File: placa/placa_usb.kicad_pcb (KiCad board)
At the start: 2 copper layers, 52.5 x 17 mm, 22 parts, among them IC1 ATMEGA16U2, P1 USB_A, P2 CONN_02X05, P3 CONN_01X06, U1 LD1117S33TR, U2 TXB0106, X1 8MHz

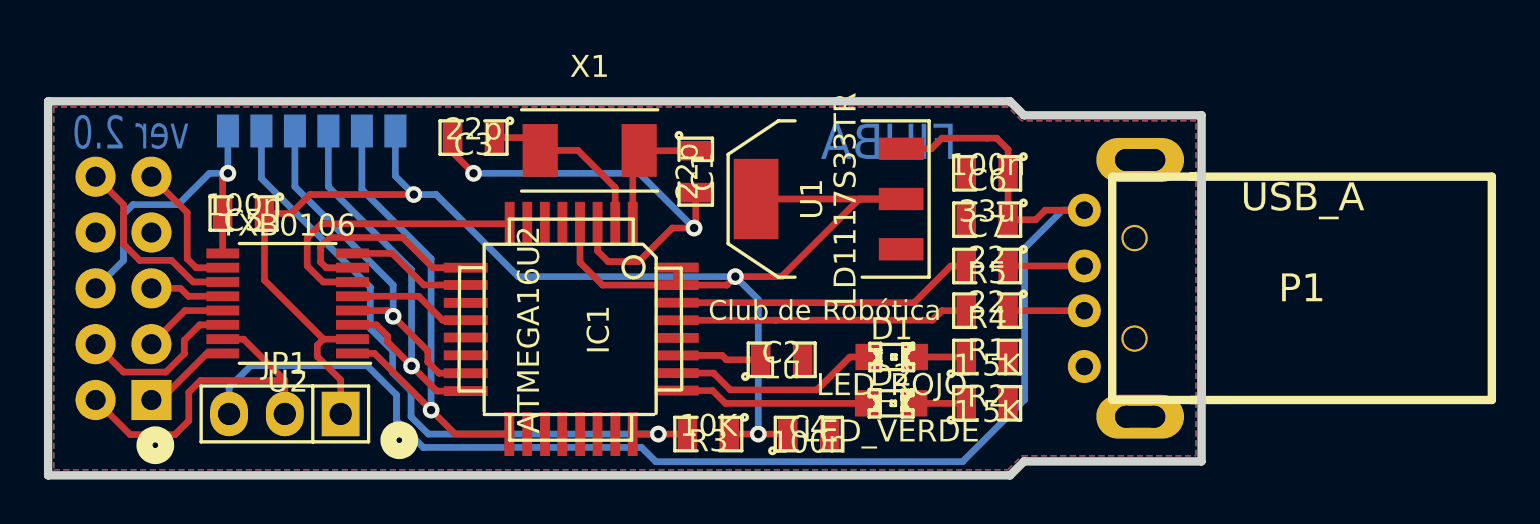
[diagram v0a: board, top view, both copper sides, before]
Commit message: primera version de la placa en componentes smd, queda verificar los tamaños de los footprint
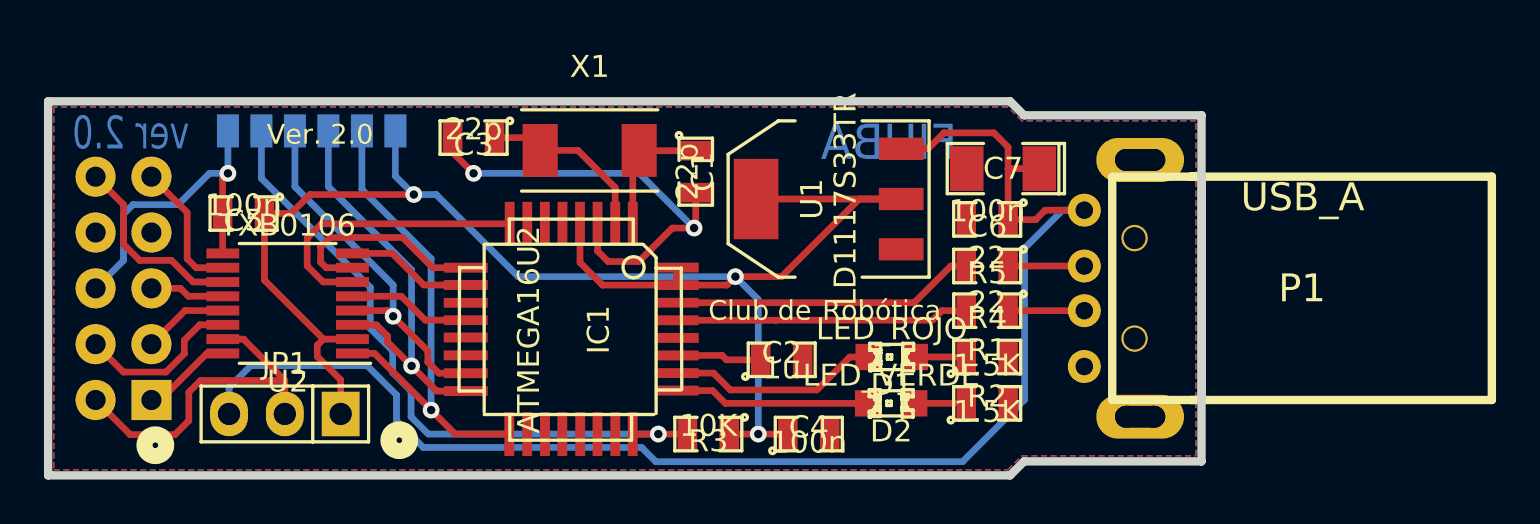
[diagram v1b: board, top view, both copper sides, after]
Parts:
- C7: footprint SMD_Packages:SMD-0805 -> SMD_Packages:SMD-1206_Pol
- moved C7 2.43 mm to (154.3, 79.6)
- moved C6 2.10 mm to (153.6, 82.0)
- turned D1 to 180 degrees
- turned D2 to 180 degrees
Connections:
- D1 pad 1: /Rojo -> Net-(D1-Pad1)
- D1 pad 2: Net-(D1-Pad2) -> /Rojo
- D2 pad 1: /Verde -> Net-(D2-Pad1)
- D2 pad 2: Net-(D2-Pad2) -> /Verde
- P1 pad 5: (no net) -> Net-(P1-Pad5)
- R1 pad 1: Net-(D1-Pad2) -> Net-(D1-Pad1)
- R2 pad 1: Net-(D2-Pad2) -> Net-(D2-Pad1)
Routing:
- net Net-(D2-Pad2): track 2.37 -> 0.00 mm
- net Net-(D2-Pad1): track 0.00 -> 2.37 mm
- net Net-(D1-Pad2): track 2.34 -> 0.00 mm
- net Net-(D1-Pad1): track 0.00 -> 2.34 mm
- net +5V: track 63.9 -> 65.6 mm
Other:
- board text added: "Ver. 2.0"
